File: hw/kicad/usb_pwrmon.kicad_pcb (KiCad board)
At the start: 2 copper layers, 23.9 x 17.5 mm, 16 parts, among them J1 16_PIN_HDR, J1 JUMPER, J2 JUMPER, J2 OLED_FPC_CONN, J3 JUMPER, J4 JUMPER, J5 JUMPER, J6 JUMPER

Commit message: - need to tune up some footprints.
Former-commit-id: 06e38749f79564db33a77a4455a47758f40de79e
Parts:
- removed the J1 at (146.1, 95.9)
- removed the J1 at (145.2, 83.4)
- removed the J2 at (144.8, 89.0)
- removed the J2 at (147.1, 83.4)
- removed J5, J6, JP7: JUMPER, jmp_small
- added C10: 0.1uF, SM0603, F.Cu at (16.5, 16.5)
- added C11: 0.1uF, SM0603, F.Cu at (19.6, 18.3)
- added C7: 2.2uF, SM0603, F.Cu at (19.6, 16.5)
- added C8: 39nF, SM0603, F.Cu at (16.5, 18.3)
- added C9: 1300pF, SM0603, F.Cu at (53.3, 16.5)
- added D1: LED, SM0603, F.Cu at (25.7, 16.5)
- added J1: ARM_10PIN, ARM_10_PIN, F.Cu at (42.2, 12.7)
- added J2: USB_MALE_A, USB_A, F.Cu at (30.7, 0.51)
- added JP1: JUMPER, jmp_small, F.Cu at (47.0, 10.7)
- added JP2: JUMPER, jmp_small, F.Cu at (45.2, 10.7)
- added J_2: OLED_FPC_CONN, oled_fpc_30, F.Cu at (45.7, -5.84)
- added R2: 25K, SM0603, F.Cu at (50.3, 16.5)
- added R3: 8K, SM0603, F.Cu at (52.6, 10.2)
- added R4: 33R, SM0603, F.Cu at (22.6, 18.3)
- added R5: 33R, SM0603, F.Cu at (25.7, 18.3)
- added R6: LVK12-SHUNT, lvk12, F.Cu at (38.9, 11.2)
- added R7: 10K, SM0603, F.Cu at (28.7, 18.3)
- added R8: 10K, SM0603, F.Cu at (34.8, 16.5)
- added R9: 330R, SM0603, F.Cu at (22.6, 16.5)
- added U1: AD8293G80, sot23-8, F.Cu at (32.8, 9.91)
- added U2: MKL24Z64VFM4, MKL24Z64VFM4, F.Cu at (28.7, 12.2)
- C1, C2, C3, C4, C5, C6: moved to F.Cu
- J3: value JUMPER -> USB_MICRO_B; footprint jmp_small -> USB_MICRO_AB
- J4: value JUMPER -> USB_FEMALE_A; footprint jmp_small -> USB_A
- R1: value 390R -> 390K; moved to F.Cu
- moved J4 158.5 mm to (16.3, 0.51), turned to 0 degrees
- moved J3 147.1 mm to (20.3, 13.0), turned to 0 degrees
- moved C1 138.4 mm to (44.2, 16.5), turned to 0 degrees
- moved C2 137.4 mm to (28.7, 16.5), turned to 0 degrees
- moved C6 137.3 mm to (47.2, 16.5), turned to 0 degrees
- moved C3 136.2 mm to (31.8, 16.5), turned to 0 degrees
- moved R1 135.6 mm to (41.1, 16.5)
- moved C5 134.1 mm to (38.1, 16.5), turned to 0 degrees
- moved C4 127.0 mm to (49.5, 10.2), turned to 0 degrees
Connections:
- J3 pad 1: BS1 -> USB_VBUS
- J3 pad 2: +3.3 -> MON_USB_DM
- J4 pad 1: BS1 -> N-0000011
- J4 pad 2: GND -> USB_DP
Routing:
- net +3.3: track 43.9 -> 0.00 mm, vias 4 -> 0
- net ~RST: track 18.2 -> 0.00 mm, vias 1 -> 0
- net ~CS: track 16.6 -> 0.00 mm, vias 1 -> 0
- net GND: track 16.2 -> 0.00 mm, vias 1 -> 0
- net R/W: track 15.7 -> 0.00 mm, vias 1 -> 0
- net D2/I2C_SDA: track 14.4 -> 0.00 mm, vias 1 -> 0
- net D1/SPI_SDIN/I2C_SDA: track 12.8 -> 0.00 mm, vias 1 -> 0
- net BS0: track 10.8 -> 0.00 mm
- net DC/I2X_SA0: track 9.14 -> 0.00 mm
- net D4: track 8.79 -> 0.00 mm
- net D0/SPI_SCLK/I2C_SCK: track 8.59 -> 0.00 mm
- net BS1: track 8.01 -> 0.00 mm
- net E/RD: track 8.00 -> 0.00 mm
- net D6: track 7.89 -> 0.00 mm
- net BS2: track 7.20 -> 0.00 mm
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- removed copper zone on B.Cu, net GND
- removed copper zone on F.Cu, net GND
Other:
- board outline removed
- board text removed: "git.io/18upyg oled_brkout v0.2"

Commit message: -add new modules for usb connectors
Former-commit-id: 8528c22d668e644492783460fc071a81398a9852 [formerly 8528c22d668e644492783460fc071a81398a9852 [formerly 8a7208a3f11d2e1f03074ef862d38f2a5259feeb]]
Former-commit-id: 9629e5bde1f754a46e235d75e6e9f8705da5d1a8
Former-commit-id: f07cc5612e676b18094e0d693e12c6ec81d661b1
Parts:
- J2: footprint USB_A -> usb_a_male_M701-280442
- J3: footprint USB_MICRO_AB -> usb_micro_b_10118193-0001LF
- J4: footprint USB_A -> usb_a_female_87520-0010BLF
- moved JP2 59.7 mm to (23.6, 66.3)
- moved JP1 49.9 mm to (50.0, 60.5)
- moved C6 49.4 mm to (21.6, 58.7)
- moved R2 49.4 mm to (24.6, 58.7)
- moved C9 49.1 mm to (28.2, 58.7)
- moved C10 44.0 mm to (47.2, 48.0)
- moved R5 43.4 mm to (41.7, 58.7)
- moved R7 43.4 mm to (44.7, 58.7)
- moved R4 43.3 mm to (38.4, 58.7)
- moved C11 43.3 mm to (35.1, 58.7)
- moved C8 43.2 mm to (31.8, 58.7)
- moved R6 42.2 mm to (29.5, 52.3)
- moved J_2 40.3 mm to (25.9, 29.2)
- moved C1 40.1 mm to (48.3, 56.4)
- moved C3 40.0 mm to (34.5, 56.4)
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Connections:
- J1 pad 6: (no net) -> N-0000028
- J1 pad 7: (no net) -> N-0000027
- J1 pad 8: (no net) -> N-0000026
- J3 pad 4: (no net) -> N-0000010
- J_2 pad 7: (no net) -> N-0000040
- U2 pad 1: (no net) -> N-0000025
- U2 pad 12: (no net) -> N-0000012
- U2 pad 14: (no net) -> N-0000023
- U2 pad 17: (no net) -> N-0000022
- U2 pad 18: (no net) -> N-0000021
- U2 pad 20: (no net) -> N-0000035
- U2 pad 21: (no net) -> N-0000020
- U2 pad 22: (no net) -> N-0000019
- U2 pad 28: (no net) -> N-0000018
- U2 pad 29: (no net) -> N-0000017
- U2 pad 30: (no net) -> N-0000016
- U2 pad 32: (no net) -> N-0000015

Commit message: -start layout
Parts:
- moved J4 80.4 mm to (122.0, 32.5), turned to 90 degrees
- moved JP1 80.0 mm to (129.5, 51.5)
- moved C1 80.0 mm to (127.8, 47.4)
- moved C11 80.0 mm to (114.6, 49.7)
- moved C2 80.0 mm to (110.7, 47.4)
- moved C3 80.0 mm to (114.0, 47.4)
- moved C5 80.0 mm to (120.4, 47.4)
- moved C6 80.0 mm to (101.1, 49.7)
- moved C7 80.0 mm to (101.1, 47.4)
- moved C8 80.0 mm to (111.2, 49.7)
- moved C9 80.0 mm to (107.7, 49.7)
- moved D1 80.0 mm to (107.7, 47.4)
- moved JP2 80.0 mm to (103.1, 57.3)
- moved R1 80.0 mm to (123.4, 47.4)
- moved R2 80.0 mm to (104.1, 49.7)
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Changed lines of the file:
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@@
     (links 104)
     (no_connects 104)
-    (area 0 0 0 0)
+    (area 19.959667 8.006 56.728333 69.023)
     (thickness 1.6)
     (drawings 0)
@@
     (pad_to_mask_clearance 0.2)
     (aux_axis_origin 0 0)
-    (visible_elements 7FFFFFBF)
+    (visible_elements 7FFFF7BF)
     (pcbplotparams
       (layerselection 284196865)
@@
   )
   (module sot23-8 (layer F.Cu)
-    (at 36.576 36.322)
+    (at 92 33.5)
     (fp_text reference U1 (at 1.651 -1.397) (layer F.SilkS) hide
       (effects (font (size 0.75 0.75) (thickness 0.15)))
@@
   )
   (module SM0603 (layer F.Cu)
-    (at 43.942 48.006)
+    (at 116.442 56.006)
     (attr smd)
     (fp_text reference R3 (at 0 0) (layer F.SilkS)
@@
   )
   (module SM0603 (layer F.Cu)
-    (at 47.244 48.006)
+    (at 119.744 56.006)
     (attr smd)
     (fp_text reference C10 (at 0 0) (layer F.SilkS)
@@
   )
   (module SM0603 (layer F.Cu)
-    (at 21.59 56.388)
+    (at 101.09 47.388)
     (attr smd)
     (fp_text reference C7 (at 0 0) (layer F.SilkS)
@@
   )
   (module SM0603 (layer F.Cu)
-    (at 24.892 56.388)
+    (at 104.392 47.388)
     (attr smd)
     (fp_text reference R9 (at 0 0) (layer F.SilkS)
@@
   )
   (module SM0603 (layer F.Cu)
-    (at 28.194 56.388)
+    (at 107.694 47.388)
     (attr smd)
     (fp_text reference D1 (at 0 0) (layer F.SilkS)
@@
   )
   (module SM0603 (layer F.Cu)
-    (at 37.592 56.388)
+    (at 117.092 47.388)
     (attr smd)
     (fp_text reference R8 (at 0 0) (layer F.SilkS)
@@
   )
   (module SM0603 (layer F.Cu)
-    (at 44.704 58.674)
+    (at 124.204 49.674)
     (attr smd)
     (fp_text reference R7 (at 0 0) (layer F.SilkS)
@@
   )
   (module SM0603 (layer F.Cu)
-    (at 41.656 58.674)
+    (at 121.156 49.674)
     (attr smd)
     (fp_text reference R5 (at 0 0) (layer F.SilkS)
@@
   )
   (module SM0603 (layer F.Cu)
-    (at 38.354 58.674)
+    (at 117.854 49.674)
     (attr smd)
     (fp_text reference R4 (at 0 0) (layer F.SilkS)
@@
   )
   (module SM0603 (layer F.Cu)
-    (at 35.052 58.674)
+    (at 114.552 49.674)
     (attr smd)
     (fp_text reference C11 (at 0 0) (layer F.SilkS)
@@
   )
   (module SM0603 (layer F.Cu)
-    (at 31.75 58.674)
+    (at 111.25 49.674)
     (attr smd)
     (fp_text reference C8 (at 0 0) (layer F.SilkS)
@@
   )
   (module SM0603 (layer F.Cu)
-    (at 28.194 58.674)
+    (at 107.694 49.674)
     (attr smd)
     (fp_text reference C9 (at 0 0) (layer F.SilkS)
@@
   )
   (module SM0603 (layer F.Cu)
-    (at 24.638 58.674)
+    (at 104.138 49.674)
     (attr smd)
     (fp_text reference R2 (at 0 0) (layer F.SilkS)
@@
   )
   (module SM0603 (layer F.Cu)
-    (at 21.59 58.674)
+    (at 101.09 49.674)
     (attr smd)
     (fp_text reference C6 (at 0 0) (layer F.SilkS)
@@
   )
   (module SM0603 (layer F.Cu)
-    (at 48.26 56.388)
+    (at 127.76 47.388)
     (attr smd)
     (fp_text reference C1 (at 0 0) (layer F.SilkS)
@@
   )
   (module SM0603 (layer F.Cu)
-    (at 43.942 56.388)
+    (at 123.442 47.388)
     (attr smd)
     (fp_text reference R1 (at 0 0) (layer F.SilkS)
@@
   )
   (module SM0603 (layer F.Cu)
-    (at 40.894 56.388)
+    (at 120.394 47.388)
     (attr smd)
     (fp_text reference C5 (at 0 0) (layer F.SilkS)
@@
   )
   (module SM0603 (layer F.Cu)
-    (at 40.894 48.006)
+    (at 113.394 56.006)
     (attr smd)
     (fp_text reference C4 (at 0 0) (layer F.SilkS)
@@
   )
   (module SM0603 (layer F.Cu)
-    (at 34.544 56.388)
+    (at 114.044 47.388)
     (attr smd)
     (fp_text reference C3 (at 0 0) (layer F.SilkS)
@@
   )
   (module SM0603 (layer F.Cu)
-    (at 31.242 56.388)
+    (at 110.742 47.388)
     (attr smd)
     (fp_text reference C2 (at 0 0) (layer F.SilkS)
@@
   )
   (module oled_fpc_30 (layer F.Cu)
-    (at 25.908 29.21)
+    (at 92 27)
     (fp_text reference J_2 (at 0 3) (layer F.SilkS)
       (effects (font (size 0.75 0.75) (thickness 0.13)))
@@
   )
   (module MKL24Z64VFM4 (layer F.Cu)
-    (at 27.178 41.148)
+    (at 101.5 37)
     (fp_text reference U2 (at 0 -6) (layer F.SilkS)
       (effects (font (size 1 1) (thickness 0.15)))
@@
   )
   (module lvk12 (layer F.Cu)
-    (at 29.464 52.324)
+    (at 86.5 35.5)
     (fp_text reference R6 (at 0 2.159) (layer F.SilkS)
       (effects (font (size 0.8 0.8) (thickness 0.1)))
@@
   )
   (module jmp_small (layer F.Cu)
-    (at 50.038 60.452)
+    (at 129.538 51.452)
     (fp_text reference JP1 (at 0 -2.032) (layer F.SilkS)
       (effects (font (size 1 1) (thickness 0.15)))
@@
   )
   (module jmp_small (layer F.Cu)
-    (at 23.622 66.294)
+    (at 103.122 57.294)
     (fp_text reference JP2 (at 0 -2.032) (layer F.SilkS)
       (effects (font (size 1 1) (thickness 0.15)))
@@
   )
   (module ARM_10_PIN (layer F.Cu)
-    (at 46.99 39.116)
+    (at 110.5 39)
     (fp_text reference J1 (at 0.5 -4) (layer F.SilkS)
       (effects (font (size 1 1) (thickness 0.15)))
@@
   )
   (module usb_a_male_M701-280442 (layer F.Cu)
-    (at 24.638 16.51)
+    (at 75 32.5)
     (fp_text reference J2 (at 0 -7.8) (layer F.SilkS) hide
       (effects (font (size 0.75 0.75) (thickness 0.15)))
@@
   )
   (module usb_micro_b_10118193-0001LF (layer F.Cu)
-    (at 51.816 31.242)
+    (at 89.5 48)
     (fp_text reference J3 (at 0 -5) (layer F.SilkS) hide
       (effects (font (size 0.75 0.75) (thickness 0.15)))
@@
   )
   (module usb_a_female_87520-0010BLF (layer F.Cu)
-    (at 43.18 16.764)
-    (fp_text reference J4 (at 0 -8) (layer F.SilkS) hide
+    (at 122 32.5 90)
+    (fp_text reference J4 (at 0 -8 90) (layer F.SilkS) hide
       (effects (font (size 0.75 0.75) (thickness 0.15)))
     )
-    (fp_text value USB_FEMALE_A (at -7 -5.42) (layer F.SilkS)
+    (fp_text value USB_FEMALE_A (at -7 -5.42 90) (layer F.SilkS)
       (effects (font (size 0.75 0.75) (thickness 0.15)))
     )
-    (pad 5 thru_hole circle (at -6.57 0) (size 2.75 2.75) (drill 2.3) (layers *.Cu *.Mask F.SilkS)
-      (net 7 GND))
-    (pad 5 thru_hole circle (at 6.57 0) (size 2.75 2.75) (drill 2.3) (layers *.Cu *.Mask F.SilkS)
-      (net 7 GND))
-    (pad 1 thru_hole rect (at -3.5 -2.71) (size 1.2 1.2) (drill 0.92) (layers *.Cu *.Mask F.SilkS)
+    (pad 5 thru_hole circle (at -6.57 0 90) (size 2.75 2.75) (drill 2.3) (layers *.Cu *.Mask F.SilkS)
+      (net 7 GND))
+    (pad 5 thru_hole circle (at 6.57 0 90) (size 2.75 2.75) (drill 2.3) (layers *.Cu *.Mask F.SilkS)
+      (net 7 GND))
+    (pad 1 thru_hole rect (at -3.5 -2.71 90) (size 1.2 1.2) (drill 0.92) (layers *.Cu *.Mask F.SilkS)
       (net 11 N-0000011))
-    (pad 4 thru_hole circle (at 3.5 -2.71) (size 1.2 1.2) (drill 0.92) (layers *.Cu *.Mask F.SilkS)
-      (net 7 GND))
-    (pad 2 thru_hole circle (at -1 -2.71) (size 1.2 1.2) (drill 0.92) (layers *.Cu *.Mask F.SilkS)
+    (pad 4 thru_hole circle (at 3.5 -2.71 90) (size 1.2 1.2) (drill 0.92) (layers *.Cu *.Mask F.SilkS)
+      (net 7 GND))
+    (pad 2 thru_hole circle (at -1 -2.71 90) (size 1.2 1.2) (drill 0.92) (layers *.Cu *.Mask F.SilkS)
       (net 46 USB_DP))
-    (pad 3 thru_hole circle (at 1 -2.71) (size 1.2 1.2) (drill 0.92) (layers *.Cu *.Mask F.SilkS)
+    (pad 3 thru_hole circle (at 1 -2.71 90) (size 1.2 1.2) (drill 0.92) (layers *.Cu *.Mask F.SilkS)
       (net 45 USB_DM))
   )

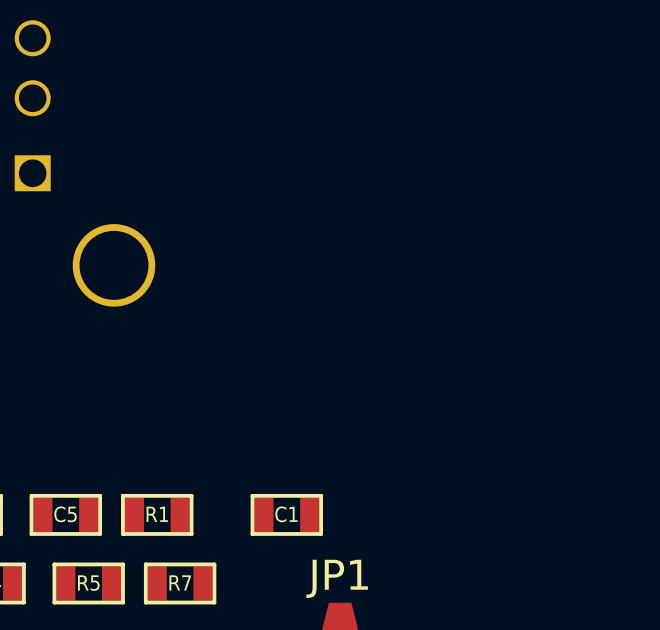
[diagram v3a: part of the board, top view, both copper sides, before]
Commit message: -add pushbutton switch
Former-commit-id: d65bfd03aaa14cbd05504ca7d7880740a1a2c356 [formerly d65bfd03aaa14cbd05504ca7d7880740a1a2c356 [formerly 96da23ec3db1ee23974b00762882926ba7f167f4]]
Former-commit-id: 3daaa6d38746a5df3fe003a87305df89f78ffee7
Former-commit-id: d47ba2748211d6b93dcb863dba6fc4110e3e7933
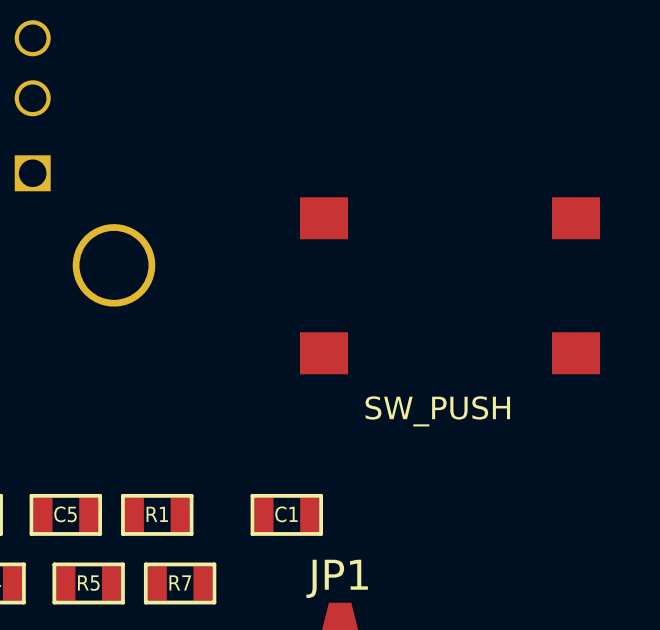
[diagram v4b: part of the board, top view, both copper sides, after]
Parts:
- added SW1: SW_PUSH, spst_pushbutton_smd, F.Cu at (129.0, 37.5)
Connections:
- net N-000001 renamed Net-<C9-Pad2>
- net N-0000010 renamed Net-<J3-Pad4>
- net N-0000011 renamed Net-<J4-Pad1>
- net N-0000012 renamed Net-<U2-Pad12>
- net N-0000013 renamed Net-<D1-Pad1>
- net N-0000015 renamed Net-<U2-Pad32>
- net N-0000016 renamed Net-<U2-Pad30>
- net N-0000018 renamed Net-<U2-Pad28>
- net N-0000019 renamed Net-<U2-Pad22>
- net N-000002 renamed Net-<C9-Pad1>
- net N-0000020 renamed Net-<U2-Pad21>
- net N-0000021 renamed Net-<U2-Pad18>
- net N-0000022 renamed Net-<U2-Pad17>
- net N-0000023 renamed Net-<U2-Pad14>
- net N-0000024 renamed Net-<D1-Pad2>
- net N-0000025 renamed Net-<U2-Pad1>
- net N-0000026 renamed Net-<J1-Pad8>
- net N-0000027 renamed Net-<J1-Pad7>
- net N-0000028 renamed Net-<J1-Pad6>
- net N-000003 renamed Net-<R2-Pad1>
- net N-0000030 renamed Net-<R7-Pad2>
- net N-0000035 renamed Net-<U2-Pad20>
- net N-0000040 renamed Net-<J_2-Pad7>
- net N-0000041 renamed Net-<C3-Pad1>
- net N-0000042 renamed Net-<C2-Pad1>
- net N-0000043 renamed Net-<C1-Pad2>
- net N-0000044 renamed Net-<J_2-Pad26>
- net N-0000045 renamed Net-<C3-Pad2>
- net N-0000046 renamed Net-<C2-Pad2>
- net N-0000048 renamed Net-<C6-Pad2>
- net N-000005 renamed Net-<R4-Pad2>
- net N-000006 renamed Net-<R5-Pad2>
- U2 pad 29: N-0000017 -> Net-<SW1-Pad2>

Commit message: - tidy up labels
Former-commit-id: 5e9b82c2bef78a302d7c585ecbd6099528578fb1
Former-commit-id: e7b477600e63daf901c13b41575262942d68aa0f
Former-commit-id: 583a5f6c1ad27e110a08d8b4af6d6768a03eff95
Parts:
- moved JP1 41.2 mm to (88.4, 49.5)
- moved JP2 10.5 mm to (96.0, 49.5)
- moved U1 8.83 mm to (84.6, 28.7)
- moved J1 7.15 mm to (103.4, 39.6), turned to 180 degrees
- moved U2 6.54 mm to (95.0, 36.3)
- moved J3 6.53 mm to (84.8, 43.4)
- moved R6 1.68 mm to (84.8, 35.3)
- moved J2 1.55 mm to (74.3, 31.1)
- moved J_2 0.89 mm to (91.7, 26.2)
